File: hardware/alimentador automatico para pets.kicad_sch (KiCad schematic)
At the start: 21 parts, among them J1 Conn_01x02, J2 Conn_01x04, J3 Conn_01x03, J4 Conn_01x03, J5 Conn_01x02, J6 Conn_01x05, J8 Conn_01x04, SW1 SW_Push, SW2 SW_Push, SW3 SW_Push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

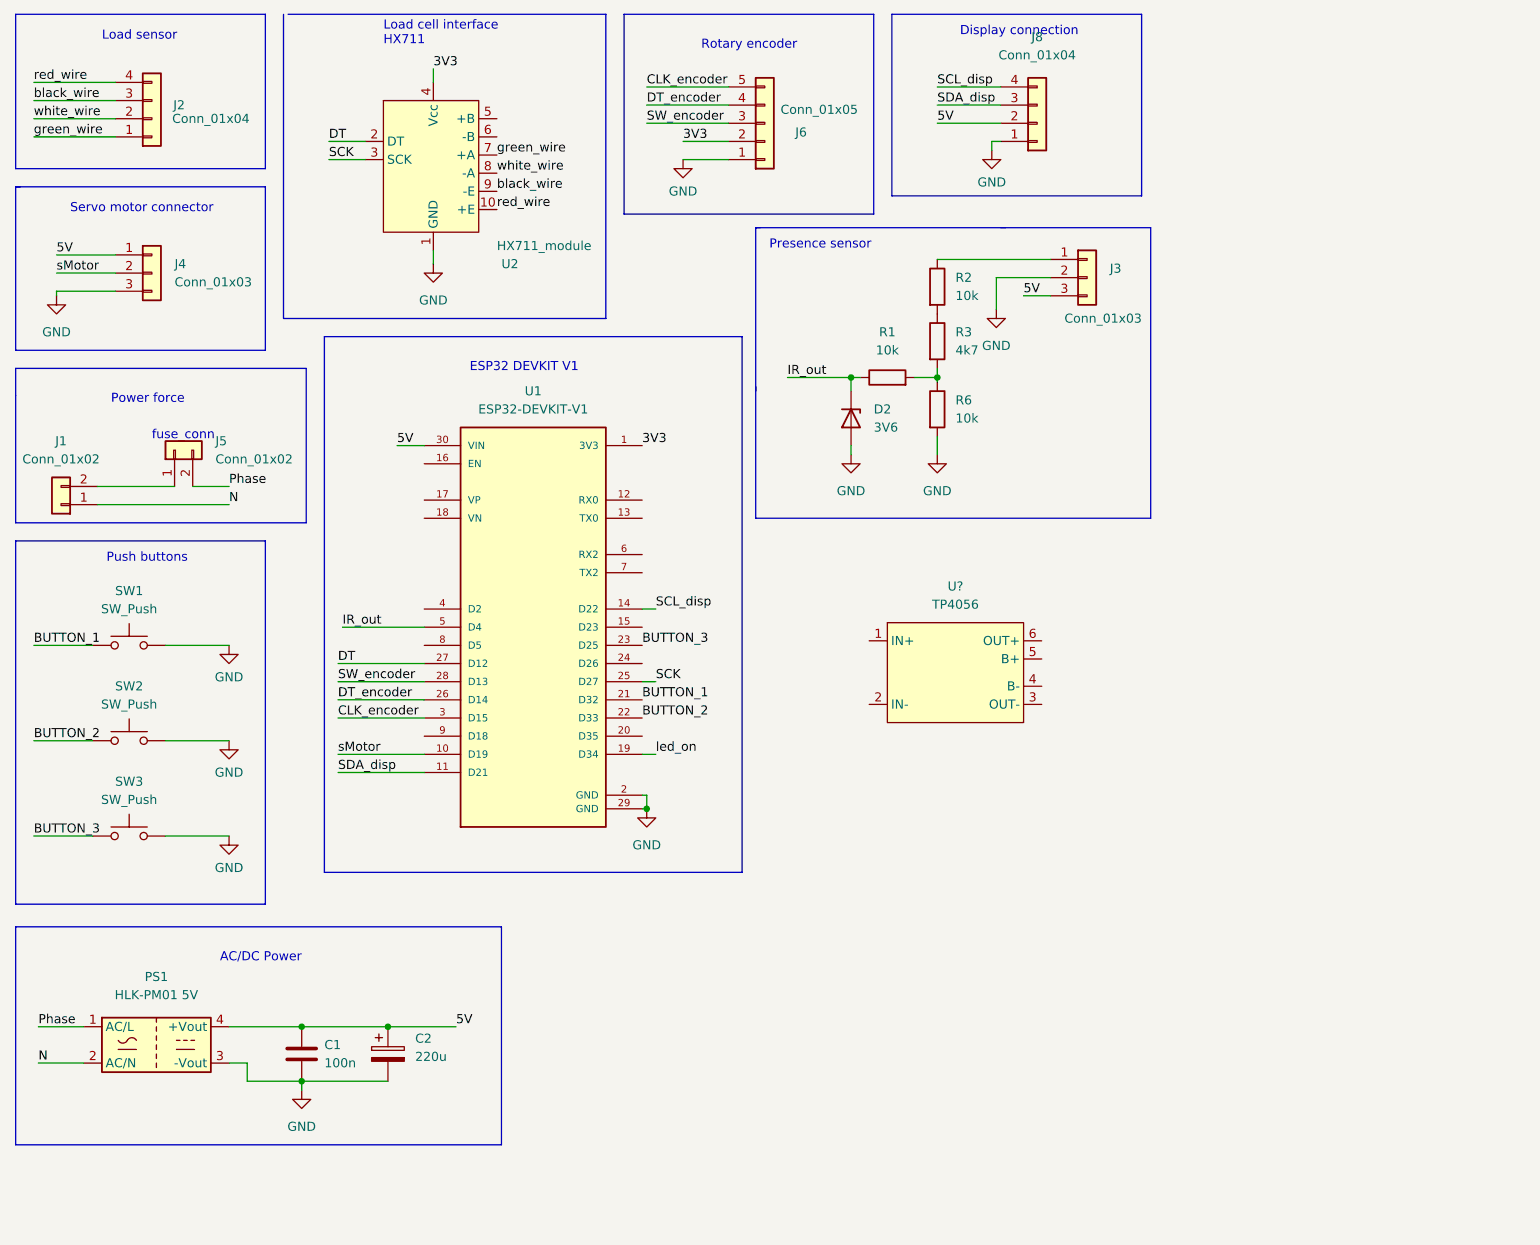
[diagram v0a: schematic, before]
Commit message: add battery module
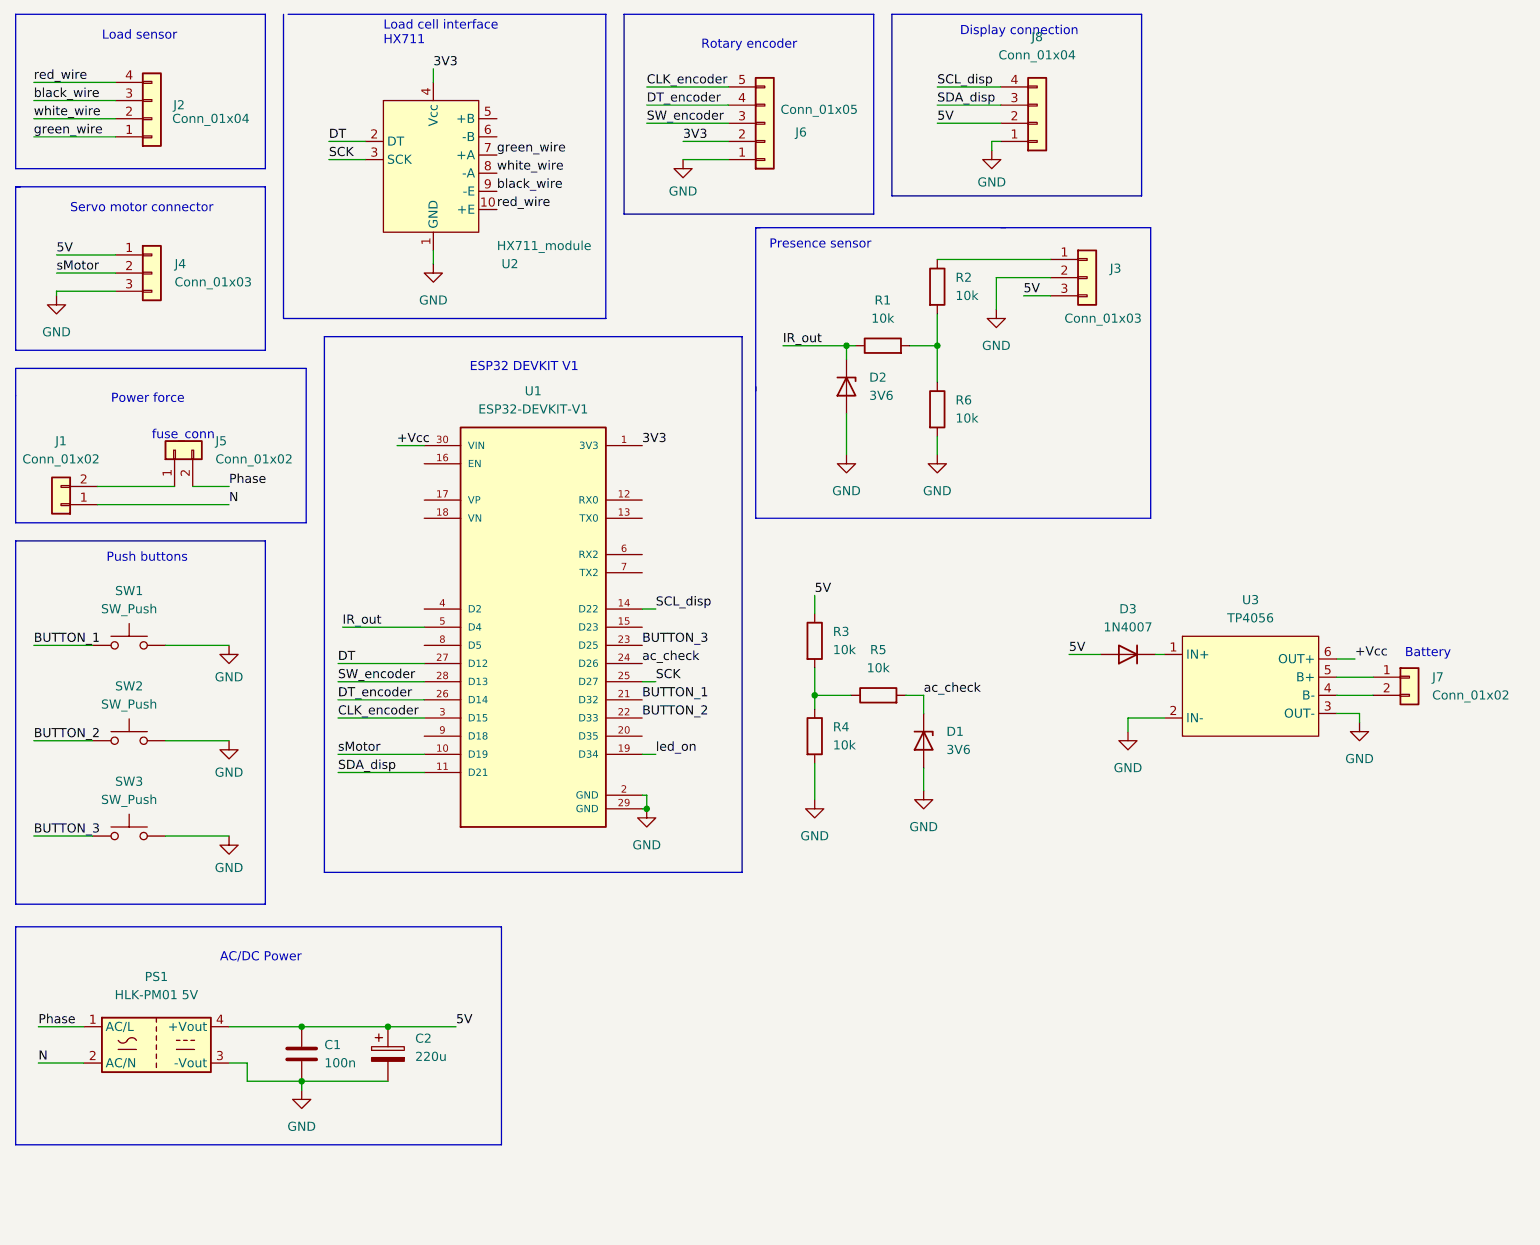
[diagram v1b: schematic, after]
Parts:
- added D1: 3V6, Diode_THT:D_DO-35_SOD27_P7.62mm_Horizontal, symbol Device:D_Zener
- added D3: 1N4007, Diode_THT:D_DO-41_SOD81_P10.16mm_Horizontal, symbol Diode:1N4007
- added J7: Conn_01x02, Connector_Wire:SolderWire-0.1sqmm_1x02_P3.6mm_D0.4mm_OD1mm_Relief, symbol Connector_Generic:Conn_01x02
- added R4, R5: 10k, Resistor_THT:R_Axial_DIN0207_L6.3mm_D2.5mm_P7.62mm_Horizontal, symbol Device:R
- R3: value 4k7 -> 10k
- U3: renamed from U?; footprint (none) -> footprint_lib:TP4056
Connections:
- net 5V: now also R3.1, D3.2 (A); no longer U1.30 (VIN)
- net GND: now also U3.2 (IN-), U3.3 (OUT-), D1.2 (A), R4.2
- net at R1.2, R6.1: now also R2.2; no longer R3.2
- net ac_check: now reaches U1.24 (D26)
- net ac_check: now also D1.1 (K), R5.2
- net at U3.1 (IN+): now also D3.1 (K)
- net at U3.4 (B-): now also J7.2 (Pin_2)
- net at U3.5 (B+): now also J7.1 (Pin_1)
- net +Vcc: now reaches U3.6 (OUT+)
- net +Vcc: now also U1.30 (VIN)
- new net: R3.2, R4.1, R5.1
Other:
- note added: "Battery"
- moved on the sheet: D2, R1, U3

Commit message: att schematic #14
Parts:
- J4: footprint Connector_PinSocket_2.54mm:PinSocket_1x03_P2.54mm_Vertical -> Connector_PinHeader_2.54mm:PinHeader_1x03_P2.54mm_Vertical
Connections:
- net 5V: now also J4.2 (Pin_2); no longer J4.1 (Pin_1)
- net sMotor: now also J4.1 (Pin_1); no longer J4.2 (Pin_2)
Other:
- note added: "AC present"
- note added: "Battery management"
- moved on the sheet: C1, C2, D3, J7, PS1, U3

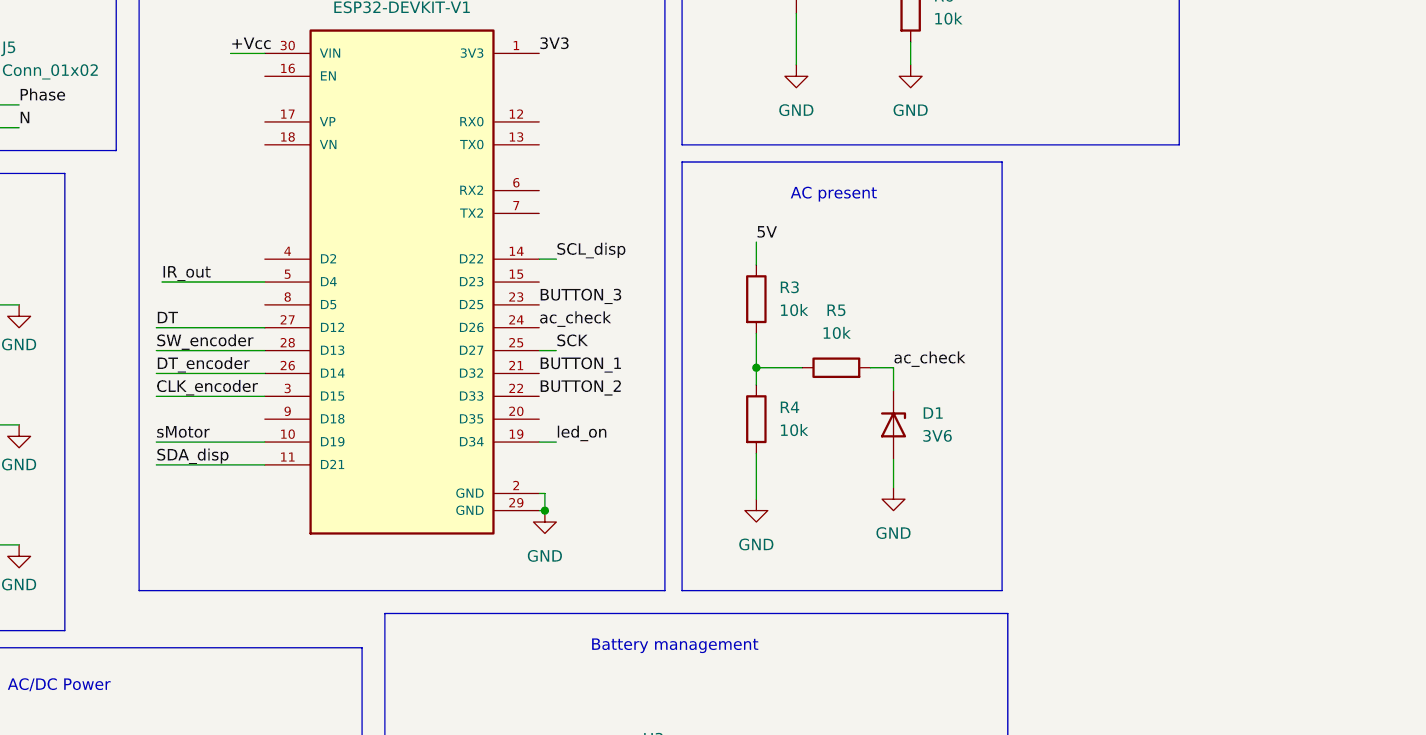
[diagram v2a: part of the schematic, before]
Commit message: added buzzer #21
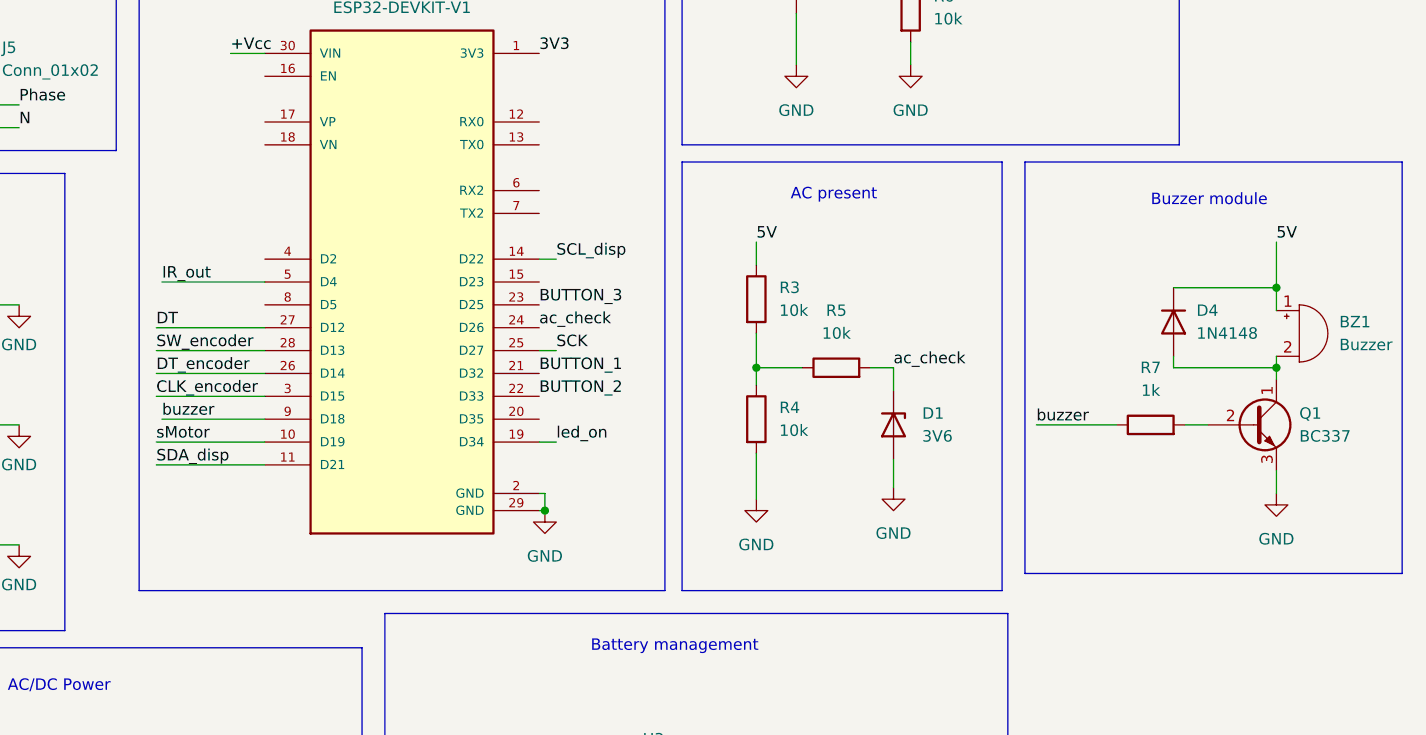
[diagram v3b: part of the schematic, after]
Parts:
- added BZ1: Buzzer, Buzzer_Beeper:Buzzer_TDK_PS1240P02BT_D12.2mm_H6.5mm, symbol Device:Buzzer
- added D4: 1N4148, Diode_THT:D_DO-35_SOD27_P7.62mm_Horizontal, symbol Diode:1N4148
- added Q1: BC337, Package_TO_SOT_THT:TO-92_Inline, symbol Transistor_BJT:BC337
- added R7: 1k, Resistor_THT:R_Axial_DIN0207_L6.3mm_D2.5mm_P7.62mm_Horizontal, symbol Device:R
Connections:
- net 5V: now also BZ1.1 (-), D4.1 (K)
- net GND: now also Q1.3 (E)
- net buzzer: now reaches U1.9 (D18)
- net buzzer: now also R7.1
- new net: BZ1.2 (+), D4.2 (A), Q1.1 (C)
- new net: Q1.2 (B), R7.2
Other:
- note added: "Buzzer module"

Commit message: place components and board roadmap #22
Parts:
- Q1: footprint Package_TO_SOT_THT:TO-92_Inline -> Package_TO_SOT_THT:TO-92L_Inline_Wide
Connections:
- net at U3.4 (B-): now also J7.1 (Pin_1); no longer J7.2 (Pin_2)
- net at U3.5 (B+): now also J7.2 (Pin_2); no longer J7.1 (Pin_1)
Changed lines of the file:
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@@
       (effects (font (size 1.27 1.27)) (justify left))
     )
-    (property "Footprint" "Package_TO_SOT_THT:TO-92_Inline" (id 2) (at 195.58 121.92 0)
+    (property "Footprint" "Package_TO_SOT_THT:TO-92L_Inline_Wide" (id 2) (at 195.58 121.92 0)
       (effects (font (size 1.27 1.27) italic) (justify left) hide)
     )
@@
     (pin "3")
   )
-  (symbol (lib_id "Connector_Generic:Conn_01x02") (at 146.05 165.735 0) (unit 1)
-    (in_bom yes) (on_board yes) (fields_autoplaced)
-    (property "Reference" "J7" (id 0) (at 149.225 165.7349 0)
-      (effects (font (size 1.27 1.27)) (justify left))
-    )
-    (property "Value" "Conn_01x02" (id 1) (at 149.225 168.2749 0)
-      (effects (font (size 1.27 1.27)) (justify left))
-    )
-    (property "Footprint" "Connector_Wire:SolderWire-0.1sqmm_1x02_P3.6mm_D0.4mm_OD1mm_Relief" (id 2) (at 146.05 165.735 0)
-      (effects (font (size 1.27 1.27)) hide)
-    )
-    (property "Datasheet" "~" (id 3) (at 146.05 165.735 0)
+  (symbol (lib_id "Connector_Generic:Conn_01x02") (at 146.05 168.275 0) (mirror x) (unit 1)
+    (in_bom yes) (on_board yes)
+    (property "Reference" "J7" (id 0) (at 149.225 169.545 0))
+    (property "Value" "Conn_01x02" (id 1) (at 150.495 172.085 0))
+    (property "Footprint" "Connector_Wire:SolderWire-0.1sqmm_1x02_P3.6mm_D0.4mm_OD1mm_Relief" (id 2) (at 146.05 168.275 0)
+      (effects (font (size 1.27 1.27)) hide)
+    )
+    (property "Datasheet" "~" (id 3) (at 146.05 168.275 0)
       (effects (font (size 1.27 1.27)) hide)
     )
@@
     )
     (path "/9af5594e-e861-4257-879d-dd72da5cd8d7"
-      (reference "Q1") (unit 1) (value "BC337") (footprint "Package_TO_SOT_THT:TO-92_Inline")
+      (reference "Q1") (unit 1) (value "BC337") (footprint "Package_TO_SOT_THT:TO-92L_Inline_Wide")
     )
     (path "/00c266d6-6426-43b2-b5e4-e389ea427658"

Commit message: pcb design review
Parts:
- removed D3: 1N4007, Diode_THT:D_DO-41_SOD81_P10.16mm_Horizontal, symbol Diode:1N4007
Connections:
- net 5V: now also U3.1 (IN+)
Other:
- moved on the sheet: D4
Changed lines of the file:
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@@
   (junction (at 63.5 158.75) (diameter 0) (color 0 0 0 0)
   )
-  (junction (at 193.04 113.665) (diameter 0) (color 0 0 0 0)
-  )
   (junction (at 63.5 166.37) (diameter 0) (color 0 0 0 0)
   )
@@
   (junction (at 135.255 113.665) (diameter 0) (color 0 0 0 0)
   )
+  (junction (at 193.04 114.3) (diameter 0) (color 0 0 0 0)
+  )
   (junction (at 139.7 64.77) (diameter 0) (color 0 0 0 0)
   )
@@
     (stroke (width 0) (type default) (color 0 0 0 0))
   )
-  (wire (pts (xy 181.61 112.395) (xy 181.61 113.665))
-    (stroke (width 0) (type default) (color 0 0 0 0))
-  )
   (polyline (pts (xy 23.495 18.415) (xy 23.495 40.005))
     (stroke (width 0) (type default) (color 0 0 0 0))
@@
     (stroke (width 0) (type default) (color 0 0 0 0))
   )
+  (wire (pts (xy 188.595 112.395) (xy 188.595 114.3))
+    (stroke (width 0) (type default) (color 0 0 0 0))
+  )
   (wire (pts (xy 111.76 28.575) (xy 123.19 28.575))
     (stroke (width 0) (type default) (color 0 0 0 0))
@@
     (stroke (width 0) (type default) (color 0 0 0 0))
   )
-  (wire (pts (xy 181.61 113.665) (xy 193.04 113.665))
-    (stroke (width 0) (type default) (color 0 0 0 0))
-  )
   (polyline (pts (xy 23.495 67.945) (xy 64.135 67.945))
     (stroke (width 0) (type default) (color 0 0 0 0))
@@
     (stroke (width 0) (type default) (color 0 0 0 0))
   )
+  (wire (pts (xy 188.595 114.3) (xy 193.04 114.3))
+    (stroke (width 0) (type default) (color 0 0 0 0))
+  )
   (polyline (pts (xy 58.42 42.545) (xy 58.42 65.405))
     (stroke (width 0) (type default) (color 0 0 0 0))
@@
     (stroke (width 0) (type default) (color 0 0 0 0))
   )
-  (wire (pts (xy 98.425 162.56) (xy 102.87 162.56))
-    (stroke (width 0) (type default) (color 0 0 0 0))
-  )
   (polyline (pts (xy 23.495 18.415) (xy 58.42 18.415))
     (stroke (width 0) (type default) (color 0 0 0 0))
@@
     (stroke (width 0) (type default) (color 0 0 0 0))
   )
-  (wire (pts (xy 181.61 104.775) (xy 193.04 104.775))
+  (wire (pts (xy 188.595 104.775) (xy 193.04 104.775))
     (stroke (width 0) (type default) (color 0 0 0 0))
   )
@@
     (stroke (width 0) (type default) (color 0 0 0 0))
   )
-  (wire (pts (xy 193.04 113.665) (xy 193.04 114.935))
-    (stroke (width 0) (type default) (color 0 0 0 0))
-  )
   (wire (pts (xy 111.76 129.54) (xy 111.76 127.635))
     (stroke (width 0) (type default) (color 0 0 0 0))
@@
     (stroke (width 0) (type default) (color 0 0 0 0))
   )
-  (wire (pts (xy 110.49 162.56) (xy 111.76 162.56))
+  (wire (pts (xy 104.775 162.56) (xy 111.76 162.56))
     (stroke (width 0) (type default) (color 0 0 0 0))
   )
@@
     (stroke (width 0) (type default) (color 0 0 0 0))
   )
+  (wire (pts (xy 193.04 114.3) (xy 193.04 114.935))
+    (stroke (width 0) (type default) (color 0 0 0 0))
+  )
   (wire (pts (xy 111.76 33.655) (xy 123.19 33.655))
     (stroke (width 0) (type default) (color 0 0 0 0))
@@
     (stroke (width 0) (type default) (color 0 0 0 0))
   )
-  (wire (pts (xy 193.04 112.395) (xy 193.04 113.665))
+  (wire (pts (xy 193.04 112.395) (xy 193.04 114.3))
     (stroke (width 0) (type default) (color 0 0 0 0))
   )
@@
     (effects (font (size 1.27 1.27)) (justify left bottom))
   )
-  (label "5V" (at 98.425 162.56 0)
+  (label "5V" (at 104.775 162.56 0)
     (effects (font (size 1.27 1.27)) (justify left bottom))
   )
@@
     (pin "1")
   )
-  (symbol (lib_id "Diode:1N4007") (at 106.68 162.56 180) (unit 1)
-    (in_bom yes) (on_board yes) (fields_autoplaced)
-    (property "Reference" "D3" (id 0) (at 106.68 156.21 0))
-    (property "Value" "1N4007" (id 1) (at 106.68 158.75 0))
-    (property "Footprint" "Diode_THT:D_DO-41_SOD81_P10.16mm_Horizontal" (id 2) (at 106.68 158.115 0)
-      (effects (font (size 1.27 1.27)) hide)
-    )
-    (property "Datasheet" "http://www.vishay.com/docs/88503/1n4001.pdf" (id 3) (at 106.68 162.56 0)
-      (effects (font (size 1.27 1.27)) hide)
-    )
-    (pin "1")
-    (pin "2")
-  )
   (symbol (lib_id "Device:R") (at 179.07 120.015 90) (unit 1)
-    (in_bom yes) (on_board yes) (fields_autoplaced)
-    (property "Reference" "R7" (id 0) (at 179.07 113.665 90))
-    (property "Value" "1k" (id 1) (at 179.07 116.205 90))
+    (in_bom yes) (on_board yes)
+    (property "Reference" "R7" (id 0) (at 179.07 114.935 90))
+    (property "Value" "1k" (id 1) (at 179.07 116.84 90))
     (property "Footprint" "Resistor_THT:R_Axial_DIN0207_L6.3mm_D2.5mm_P7.62mm_Horizontal" (id 2) (at 179.07 121.793 90)
       (effects (font (size 1.27 1.27)) hide)
@@
     (pin "2")
   )
-  (symbol (lib_id "Diode:1N4148") (at 181.61 108.585 270) (unit 1)
-    (in_bom yes) (on_board yes) (fields_autoplaced)
-    (property "Reference" "D4" (id 0) (at 184.15 107.3149 90)
-      (effects (font (size 1.27 1.27)) (justify left))
-    )
-    (property "Value" "1N4148" (id 1) (at 184.15 109.8549 90)
-      (effects (font (size 1.27 1.27)) (justify left))
-    )
-    (property "Footprint" "Diode_THT:D_DO-35_SOD27_P7.62mm_Horizontal" (id 2) (at 177.165 108.585 0)
-      (effects (font (size 1.27 1.27)) hide)
-    )
-    (property "Datasheet" "https://assets.nexperia.com/documents/data-sheet/1N4148_1N4448.pdf" (id 3) (at 181.61 108.585 0)
+  (symbol (lib_id "Diode:1N4148") (at 188.595 108.585 270) (unit 1)
+    (in_bom yes) (on_board yes)
+    (property "Reference" "D4" (id 0) (at 182.245 107.315 90)
+      (effects (font (size 1.27 1.27)) (justify left))
+    )
+    (property "Value" "1N4148" (id 1) (at 179.07 109.855 90)
+      (effects (font (size 1.27 1.27)) (justify left))
+    )
+    (property "Footprint" "Diode_THT:D_DO-35_SOD27_P7.62mm_Horizontal" (id 2) (at 184.15 108.585 0)
+      (effects (font (size 1.27 1.27)) hide)
+    )
+    (property "Datasheet" "https://assets.nexperia.com/documents/data-sheet/1N4148_1N4448.pdf" (id 3) (at 188.595 108.585 0)
       (effects (font (size 1.27 1.27)) hide)
     )
@@
       (reference "D2") (unit 1) (value "3V6") (footprint "Diode_THT:D_DO-35_SOD27_P7.62mm_Horizontal")
     )
-    (path "/73135535-2a02-4874-8de9-ac02be991519"
-      (reference "D3") (unit 1) (value "1N4007") (footprint "Diode_THT:D_DO-41_SOD81_P10.16mm_Horizontal")
-    )
     (path "/d6bd327a-d697-404f-a5b7-0c1f2f1bf9b6"
